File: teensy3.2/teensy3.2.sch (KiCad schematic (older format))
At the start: 30 parts

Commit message: ERC ok
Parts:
- removed Y?: 16 MHz, symbol Device:Crystal
- added C10, C11, C5, C6, C7: 0.1uF, symbol Device:CP_Small
- added C8, C9: 2.2uF, symbol Device:CP_Small
- added FB1, FB2: Ferrite, symbol Device:Ferrite_Bead
- added J12: AGND, TestPoint:TestPoint_Bridge_Pitch2.0mm_Drill0.7mm, symbol Connector_Generic:Conn_01x01
- added J13: AREF, TestPoint:TestPoint_Bridge_Pitch2.0mm_Drill0.7mm, symbol Connector_Generic:Conn_01x01
- added J14: 31, TestPoint:TestPoint_Bridge_Pitch2.0mm_Drill0.7mm, symbol Connector_Generic:Conn_01x01
- added J15: 26, TestPoint:TestPoint_Bridge_Pitch2.0mm_Drill0.7mm, symbol Connector_Generic:Conn_01x01
- added J16: A10, TestPoint:TestPoint_Bridge_Pitch2.0mm_Drill0.7mm, symbol Connector_Generic:Conn_01x01
- added J17: A11, TestPoint:TestPoint_Bridge_Pitch2.0mm_Drill0.7mm, symbol Connector_Generic:Conn_01x01
- added J18: A12, TestPoint:TestPoint_Bridge_Pitch2.0mm_Drill0.7mm, symbol Connector_Generic:Conn_01x01
- added J19: A13, TestPoint:TestPoint_Bridge_Pitch2.0mm_Drill0.7mm, symbol Connector_Generic:Conn_01x01
- added J20: 33, TestPoint:TestPoint_Bridge_Pitch2.0mm_Drill0.7mm, symbol Connector_Generic:Conn_01x01
- added J21: 24, TestPoint:TestPoint_Bridge_Pitch2.0mm_Drill0.7mm, symbol Connector_Generic:Conn_01x01
- added J22: 3, TestPoint:TestPoint_Bridge_Pitch2.0mm_Drill0.7mm, symbol Connector_Generic:Conn_01x01
- added J23: 4, TestPoint:TestPoint_Bridge_Pitch2.0mm_Drill0.7mm, symbol Connector_Generic:Conn_01x01
- added J25: DAC/A14, TestPoint:TestPoint_Bridge_Pitch2.0mm_Drill0.7mm, symbol Connector_Generic:Conn_01x01
- added J26: 16/A2, TestPoint:TestPoint_Bridge_Pitch2.0mm_Drill0.7mm, symbol Connector_Generic:Conn_01x01
- added J27: 17/A3, TestPoint:TestPoint_Bridge_Pitch2.0mm_Drill0.7mm, symbol Connector_Generic:Conn_01x01
- added J28: 19/A5, TestPoint:TestPoint_Bridge_Pitch2.0mm_Drill0.7mm, symbol Connector_Generic:Conn_01x01
- added J29: 18/A4, TestPoint:TestPoint_Bridge_Pitch2.0mm_Drill0.7mm, symbol Connector_Generic:Conn_01x01
- added J30: 0, TestPoint:TestPoint_Bridge_Pitch2.0mm_Drill0.7mm, symbol Connector_Generic:Conn_01x01
- added J31: 1, TestPoint:TestPoint_Bridge_Pitch2.0mm_Drill0.7mm, symbol Connector_Generic:Conn_01x01
- added J32: 32, TestPoint:TestPoint_Bridge_Pitch2.0mm_Drill0.7mm, symbol Connector_Generic:Conn_01x01
- added J33: 25, TestPoint:TestPoint_Bridge_Pitch2.0mm_Drill0.7mm, symbol Connector_Generic:Conn_01x01
- added J34: 15/A1, TestPoint:TestPoint_Bridge_Pitch2.0mm_Drill0.7mm, symbol Connector_Generic:Conn_01x01
- added J35: 22/A8, TestPoint:TestPoint_Bridge_Pitch2.0mm_Drill0.7mm, symbol Connector_Generic:Conn_01x01
- added J36: 23/A9, TestPoint:TestPoint_Bridge_Pitch2.0mm_Drill0.7mm, symbol Connector_Generic:Conn_01x01
- added J37: 9, TestPoint:TestPoint_Bridge_Pitch2.0mm_Drill0.7mm, symbol Connector_Generic:Conn_01x01
- added J38: 10, TestPoint:TestPoint_Bridge_Pitch2.0mm_Drill0.7mm, symbol Connector_Generic:Conn_01x01
- added J39: 11, TestPoint:TestPoint_Bridge_Pitch2.0mm_Drill0.7mm, symbol Connector_Generic:Conn_01x01
- added J40: 12, TestPoint:TestPoint_Bridge_Pitch2.0mm_Drill0.7mm, symbol Connector_Generic:Conn_01x01
- added J41: 28, TestPoint:TestPoint_Bridge_Pitch2.0mm_Drill0.7mm, symbol Connector_Generic:Conn_01x01
- added J42: 27, TestPoint:TestPoint_Bridge_Pitch2.0mm_Drill0.7mm, symbol Connector_Generic:Conn_01x01
- added J43: 29, TestPoint:TestPoint_Bridge_Pitch2.0mm_Drill0.7mm, symbol Connector_Generic:Conn_01x01
- added J44: 30, TestPoint:TestPoint_Bridge_Pitch2.0mm_Drill0.7mm, symbol Connector_Generic:Conn_01x01
- added J45: 2, TestPoint:TestPoint_Bridge_Pitch2.0mm_Drill0.7mm, symbol Connector_Generic:Conn_01x01
- added J46: 14/A0, TestPoint:TestPoint_Bridge_Pitch2.0mm_Drill0.7mm, symbol Connector_Generic:Conn_01x01
- added J47: 7, TestPoint:TestPoint_Bridge_Pitch2.0mm_Drill0.7mm, symbol Connector_Generic:Conn_01x01
- added J48: 8, TestPoint:TestPoint_Bridge_Pitch2.0mm_Drill0.7mm, symbol Connector_Generic:Conn_01x01
- added J49: 6, TestPoint:TestPoint_Bridge_Pitch2.0mm_Drill0.7mm, symbol Connector_Generic:Conn_01x01
- added J50: 20/A6, TestPoint:TestPoint_Bridge_Pitch2.0mm_Drill0.7mm, symbol Connector_Generic:Conn_01x01
- added J51: 21/A7, TestPoint:TestPoint_Bridge_Pitch2.0mm_Drill0.7mm, symbol Connector_Generic:Conn_01x01
- added J52: 5, TestPoint:TestPoint_Bridge_Pitch2.0mm_Drill0.7mm, symbol Connector_Generic:Conn_01x01
- added J7: 3.3V, TestPoint:TestPoint_Bridge_Pitch2.0mm_Drill0.7mm, symbol Connector_Generic:Conn_01x01
- added R3: 470, symbol Device:R
- added Y2: 16 MHz, symbol Device:Crystal
- gave numbers to parts that had none: 29
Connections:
- net labels added: GNDA, PTA0, PTA1, PTA2, PTA3, VBAT
- wire segments 110 -> 197
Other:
- moved on the sheet: C1, C2, C3, C4, D1, D2, D3, F1, J1, J10, J11, J2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

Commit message: asignacion de footprints lista
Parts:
- removed D1, D2: 1A, symbol Device:D
- removed FB1, FB2: Ferrite, symbol Device:Ferrite_Bead
- removed J10, J9: GND, TestPoint:TestPoint_Bridge_Pitch2.0mm_Drill0.7mm, symbol Connector_Generic:Conn_01x01
- removed J11: PROG, TestPoint:TestPoint_Bridge_Pitch2.0mm_Drill0.7mm, symbol Connector_Generic:Conn_01x01
- removed J12: AGND, TestPoint:TestPoint_Bridge_Pitch2.0mm_Drill0.7mm, symbol Connector_Generic:Conn_01x01
- removed J13: AREF, TestPoint:TestPoint_Bridge_Pitch2.0mm_Drill0.7mm, symbol Connector_Generic:Conn_01x01
- removed J14: 31, TestPoint:TestPoint_Bridge_Pitch2.0mm_Drill0.7mm, symbol Connector_Generic:Conn_01x01
- removed J15: 26, TestPoint:TestPoint_Bridge_Pitch2.0mm_Drill0.7mm, symbol Connector_Generic:Conn_01x01
- removed J16: A10, TestPoint:TestPoint_Bridge_Pitch2.0mm_Drill0.7mm, symbol Connector_Generic:Conn_01x01
- removed J17: A11, TestPoint:TestPoint_Bridge_Pitch2.0mm_Drill0.7mm, symbol Connector_Generic:Conn_01x01
- removed J18: A12, TestPoint:TestPoint_Bridge_Pitch2.0mm_Drill0.7mm, symbol Connector_Generic:Conn_01x01
- removed J19: A13, TestPoint:TestPoint_Bridge_Pitch2.0mm_Drill0.7mm, symbol Connector_Generic:Conn_01x01
- removed J20: 33, TestPoint:TestPoint_Bridge_Pitch2.0mm_Drill0.7mm, symbol Connector_Generic:Conn_01x01
- removed J21: 24, TestPoint:TestPoint_Bridge_Pitch2.0mm_Drill0.7mm, symbol Connector_Generic:Conn_01x01
- removed J22: 3, TestPoint:TestPoint_Bridge_Pitch2.0mm_Drill0.7mm, symbol Connector_Generic:Conn_01x01
- removed J23: 4, TestPoint:TestPoint_Bridge_Pitch2.0mm_Drill0.7mm, symbol Connector_Generic:Conn_01x01
- removed J24: RESET, TestPoint:TestPoint_Bridge_Pitch2.0mm_Drill0.7mm, symbol Connector_Generic:Conn_01x01
- removed J25: DAC/A14, TestPoint:TestPoint_Bridge_Pitch2.0mm_Drill0.7mm, symbol Connector_Generic:Conn_01x01
- removed J26: 16/A2, TestPoint:TestPoint_Bridge_Pitch2.0mm_Drill0.7mm, symbol Connector_Generic:Conn_01x01
- removed J27: 17/A3, TestPoint:TestPoint_Bridge_Pitch2.0mm_Drill0.7mm, symbol Connector_Generic:Conn_01x01
- removed J28: 19/A5, TestPoint:TestPoint_Bridge_Pitch2.0mm_Drill0.7mm, symbol Connector_Generic:Conn_01x01
- removed J29: 18/A4, TestPoint:TestPoint_Bridge_Pitch2.0mm_Drill0.7mm, symbol Connector_Generic:Conn_01x01
- removed J3: VUSB, TestPoint:TestPoint_Bridge_Pitch2.0mm_Drill0.7mm, symbol Connector_Generic:Conn_01x01
- removed J30: 0, TestPoint:TestPoint_Bridge_Pitch2.0mm_Drill0.7mm, symbol Connector_Generic:Conn_01x01
- removed J31: 1, TestPoint:TestPoint_Bridge_Pitch2.0mm_Drill0.7mm, symbol Connector_Generic:Conn_01x01
- removed J32: 32, TestPoint:TestPoint_Bridge_Pitch2.0mm_Drill0.7mm, symbol Connector_Generic:Conn_01x01
- removed J33: 25, TestPoint:TestPoint_Bridge_Pitch2.0mm_Drill0.7mm, symbol Connector_Generic:Conn_01x01
- removed J34: 15/A1, TestPoint:TestPoint_Bridge_Pitch2.0mm_Drill0.7mm, symbol Connector_Generic:Conn_01x01
- removed J35: 22/A8, TestPoint:TestPoint_Bridge_Pitch2.0mm_Drill0.7mm, symbol Connector_Generic:Conn_01x01
- removed J36: 23/A9, TestPoint:TestPoint_Bridge_Pitch2.0mm_Drill0.7mm, symbol Connector_Generic:Conn_01x01
- removed J37: 9, TestPoint:TestPoint_Bridge_Pitch2.0mm_Drill0.7mm, symbol Connector_Generic:Conn_01x01
- removed J38: 10, TestPoint:TestPoint_Bridge_Pitch2.0mm_Drill0.7mm, symbol Connector_Generic:Conn_01x01
- removed J39: 11, TestPoint:TestPoint_Bridge_Pitch2.0mm_Drill0.7mm, symbol Connector_Generic:Conn_01x01
- removed J40: 12, TestPoint:TestPoint_Bridge_Pitch2.0mm_Drill0.7mm, symbol Connector_Generic:Conn_01x01
- removed J41: 28, TestPoint:TestPoint_Bridge_Pitch2.0mm_Drill0.7mm, symbol Connector_Generic:Conn_01x01
- removed J42: 27, TestPoint:TestPoint_Bridge_Pitch2.0mm_Drill0.7mm, symbol Connector_Generic:Conn_01x01
- removed J43: 29, TestPoint:TestPoint_Bridge_Pitch2.0mm_Drill0.7mm, symbol Connector_Generic:Conn_01x01
- removed J44: 30, TestPoint:TestPoint_Bridge_Pitch2.0mm_Drill0.7mm, symbol Connector_Generic:Conn_01x01
- removed J45: 2, TestPoint:TestPoint_Bridge_Pitch2.0mm_Drill0.7mm, symbol Connector_Generic:Conn_01x01
- removed J46: 14/A0, TestPoint:TestPoint_Bridge_Pitch2.0mm_Drill0.7mm, symbol Connector_Generic:Conn_01x01
- removed J47: 7, TestPoint:TestPoint_Bridge_Pitch2.0mm_Drill0.7mm, symbol Connector_Generic:Conn_01x01
- removed J48: 8, TestPoint:TestPoint_Bridge_Pitch2.0mm_Drill0.7mm, symbol Connector_Generic:Conn_01x01
- removed J49: 6, TestPoint:TestPoint_Bridge_Pitch2.0mm_Drill0.7mm, symbol Connector_Generic:Conn_01x01
- removed J5, J7: 3.3V, TestPoint:TestPoint_Bridge_Pitch2.0mm_Drill0.7mm, symbol Connector_Generic:Conn_01x01
- removed J50: 20/A6, TestPoint:TestPoint_Bridge_Pitch2.0mm_Drill0.7mm, symbol Connector_Generic:Conn_01x01
- removed J51: 21/A7, TestPoint:TestPoint_Bridge_Pitch2.0mm_Drill0.7mm, symbol Connector_Generic:Conn_01x01
- removed J52: 5, TestPoint:TestPoint_Bridge_Pitch2.0mm_Drill0.7mm, symbol Connector_Generic:Conn_01x01
- removed J53: 13 (LED), TestPoint:TestPoint_Bridge_Pitch2.0mm_Drill0.7mm, symbol Connector_Generic:Conn_01x01
- removed J6: VIN, TestPoint:TestPoint_Bridge_Pitch2.0mm_Drill0.7mm, symbol Connector_Generic:Conn_01x01
- removed JP1: Split VIN-VUSB, symbol Device:Jumper_NC_Small
- added D1: PMEG4010CPA, Package_SON:HUSON-3-1EP_2x2mm_P1.3mm_EP1.1x1.6mm, symbol Device:D_Schottky_x2_KCom_AAK
- added JP1: Split VIN-VUSB, Jumper:SolderJumper-2_P1.3mm_Bridged2Bar_Pad1.0x1.5mm, symbol Jumper:SolderJumper_2_Bridged
- added L1, L2: Ferrite, Inductor_SMD:L_0201_0603Metric, symbol Device:L_Core_Ferrite
- added TP10: PROG, TestPoint:TestPoint_THTPad_D2.0mm_Drill1.0mm, symbol Connector:TestPoint
- added TP11: AGND, TestPoint:TestPoint_THTPad_D2.0mm_Drill1.0mm, symbol Connector:TestPoint
- added TP12: AREF, TestPoint:TestPoint_THTPad_D2.0mm_Drill1.0mm, symbol Connector:TestPoint
- added TP13: RESET, TestPoint:TestPoint_THTPad_D2.0mm_Drill1.0mm, symbol Connector:TestPoint
- added TP14: 31, TestPoint:TestPoint_THTPad_D2.0mm_Drill1.0mm, symbol Connector:TestPoint
- added TP15: 26, TestPoint:TestPoint_THTPad_D2.0mm_Drill1.0mm, symbol Connector:TestPoint
- added TP16: A10, TestPoint:TestPoint_THTPad_D2.0mm_Drill1.0mm, symbol Connector:TestPoint
- added TP17: A11, TestPoint:TestPoint_THTPad_D2.0mm_Drill1.0mm, symbol Connector:TestPoint
- added TP18: A12, TestPoint:TestPoint_THTPad_D2.0mm_Drill1.0mm, symbol Connector:TestPoint
- added TP19: A13, TestPoint:TestPoint_THTPad_D2.0mm_Drill1.0mm, symbol Connector:TestPoint
- added TP2: VUSB, TestPoint:TestPoint_THTPad_D2.0mm_Drill1.0mm, symbol Connector:TestPoint
- added TP20: 33, TestPoint:TestPoint_THTPad_D2.0mm_Drill1.0mm, symbol Connector:TestPoint
- added TP21: 24, TestPoint:TestPoint_THTPad_D2.0mm_Drill1.0mm, symbol Connector:TestPoint
- added TP22: 3, TestPoint:TestPoint_THTPad_D2.0mm_Drill1.0mm, symbol Connector:TestPoint
- added TP23: 4, TestPoint:TestPoint_THTPad_D2.0mm_Drill1.0mm, symbol Connector:TestPoint
- added TP24: DAC/A14, TestPoint:TestPoint_THTPad_D2.0mm_Drill1.0mm, symbol Connector:TestPoint
- added TP25: 16/A2, TestPoint:TestPoint_THTPad_D2.0mm_Drill1.0mm, symbol Connector:TestPoint
- added TP26: 17/A3, TestPoint:TestPoint_THTPad_D2.0mm_Drill1.0mm, symbol Connector:TestPoint
- added TP27: 19/A5, TestPoint:TestPoint_THTPad_D2.0mm_Drill1.0mm, symbol Connector:TestPoint
- added TP28: 18/A4, TestPoint:TestPoint_THTPad_D2.0mm_Drill1.0mm, symbol Connector:TestPoint
- added TP29: 0, TestPoint:TestPoint_THTPad_D2.0mm_Drill1.0mm, symbol Connector:TestPoint
- added TP30: 1, TestPoint:TestPoint_THTPad_D2.0mm_Drill1.0mm, symbol Connector:TestPoint
- added TP31: 32, TestPoint:TestPoint_THTPad_D2.0mm_Drill1.0mm, symbol Connector:TestPoint
- added TP32: 25, TestPoint:TestPoint_THTPad_D2.0mm_Drill1.0mm, symbol Connector:TestPoint
- added TP33: 15/A1, TestPoint:TestPoint_THTPad_D2.0mm_Drill1.0mm, symbol Connector:TestPoint
- added TP34: 22/A8, TestPoint:TestPoint_THTPad_D2.0mm_Drill1.0mm, symbol Connector:TestPoint
- added TP35: 23/A9, TestPoint:TestPoint_THTPad_D2.0mm_Drill1.0mm, symbol Connector:TestPoint
- added TP36: 9, TestPoint:TestPoint_THTPad_D2.0mm_Drill1.0mm, symbol Connector:TestPoint
- added TP37: 10, TestPoint:TestPoint_THTPad_D2.0mm_Drill1.0mm, symbol Connector:TestPoint
- added TP38: 11, TestPoint:TestPoint_THTPad_D2.0mm_Drill1.0mm, symbol Connector:TestPoint
- added TP39: 12, TestPoint:TestPoint_THTPad_D2.0mm_Drill1.0mm, symbol Connector:TestPoint
- added TP4, TP6: 3.3V, TestPoint:TestPoint_THTPad_D2.0mm_Drill1.0mm, symbol Connector:TestPoint
- added TP40: 28, TestPoint:TestPoint_THTPad_D2.0mm_Drill1.0mm, symbol Connector:TestPoint
- added TP41: 27, TestPoint:TestPoint_THTPad_D2.0mm_Drill1.0mm, symbol Connector:TestPoint
- added TP42: 29, TestPoint:TestPoint_THTPad_D2.0mm_Drill1.0mm, symbol Connector:TestPoint
- added TP43: 30, TestPoint:TestPoint_THTPad_D2.0mm_Drill1.0mm, symbol Connector:TestPoint
- added TP44: 2, TestPoint:TestPoint_THTPad_D2.0mm_Drill1.0mm, symbol Connector:TestPoint
- added TP45: 14/A0, TestPoint:TestPoint_THTPad_D2.0mm_Drill1.0mm, symbol Connector:TestPoint
- added TP46: 7, TestPoint:TestPoint_THTPad_D2.0mm_Drill1.0mm, symbol Connector:TestPoint
- added TP47: 8, TestPoint:TestPoint_THTPad_D2.0mm_Drill1.0mm, symbol Connector:TestPoint
- added TP48: 6, TestPoint:TestPoint_THTPad_D2.0mm_Drill1.0mm, symbol Connector:TestPoint
- added TP49: 20/A6, TestPoint:TestPoint_THTPad_D2.0mm_Drill1.0mm, symbol Connector:TestPoint
- added TP5: VIN, TestPoint:TestPoint_THTPad_D2.0mm_Drill1.0mm, symbol Connector:TestPoint
- added TP50: 21/A7, TestPoint:TestPoint_THTPad_D2.0mm_Drill1.0mm, symbol Connector:TestPoint
- added TP51: 5, TestPoint:TestPoint_THTPad_D2.0mm_Drill1.0mm, symbol Connector:TestPoint
- added TP52: 13 (LED), TestPoint:TestPoint_THTPad_D2.0mm_Drill1.0mm, symbol Connector:TestPoint
- added TP8, TP9: GND, TestPoint:TestPoint_THTPad_D2.0mm_Drill1.0mm, symbol Connector:TestPoint
- C1, C10, C11, C5, C6, C7: footprint (none) -> Capacitor_SMD:C_0603_1608Metric
- C2, C3, C4, C8, C9: footprint (none) -> Capacitor_SMD:C_0805_2012Metric
- D2: renamed from D3; footprint (none) -> LED_SMD:LED_0805_2012Metric
- F1: footprint (none) -> Fuse:Fuse_0805_2012Metric
- J2: footprint (none) -> Connector_USB:USB_Micro-B_Molex_47346-0001
- R1, R2, R3, R4: footprint (none) -> Resistor_SMD:R_0201_0603Metric
- SW1: footprint (none) -> Button_Switch_SMD:SW_SPST_PTS810
- TP1: renamed from J1; footprint TestPoint:TestPoint_Bridge_Pitch2.0mm_Drill0.7mm -> TestPoint:TestPoint_THTPad_D2.0mm_Drill1.0mm; symbol Connector_Generic:Conn_01x01 -> Connector:TestPoint
- TP3: renamed from J4; footprint TestPoint:TestPoint_Bridge_Pitch2.0mm_Drill0.7mm -> TestPoint:TestPoint_THTPad_D2.0mm_Drill1.0mm; symbol Connector_Generic:Conn_01x01 -> Connector:TestPoint
- TP7: renamed from J8; footprint TestPoint:TestPoint_Bridge_Pitch2.0mm_Drill0.7mm -> TestPoint:TestPoint_THTPad_D2.0mm_Drill1.0mm; symbol Connector_Generic:Conn_01x01 -> Connector:TestPoint
- U3: footprint (none) -> Package_QFP:LQFP-64_10x10mm_P0.5mm
- Y1: footprint (none) -> Crystal:Crystal_SMD_TXC_AX_8045-2Pin_8.0x4.5mm
- Y2: footprint (none) -> Crystal:Crystal_SMD_HC49-SD
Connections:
- wire segments 197 -> 196
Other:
- moved on the sheet: C1, C2, C5, C6, C7, C8

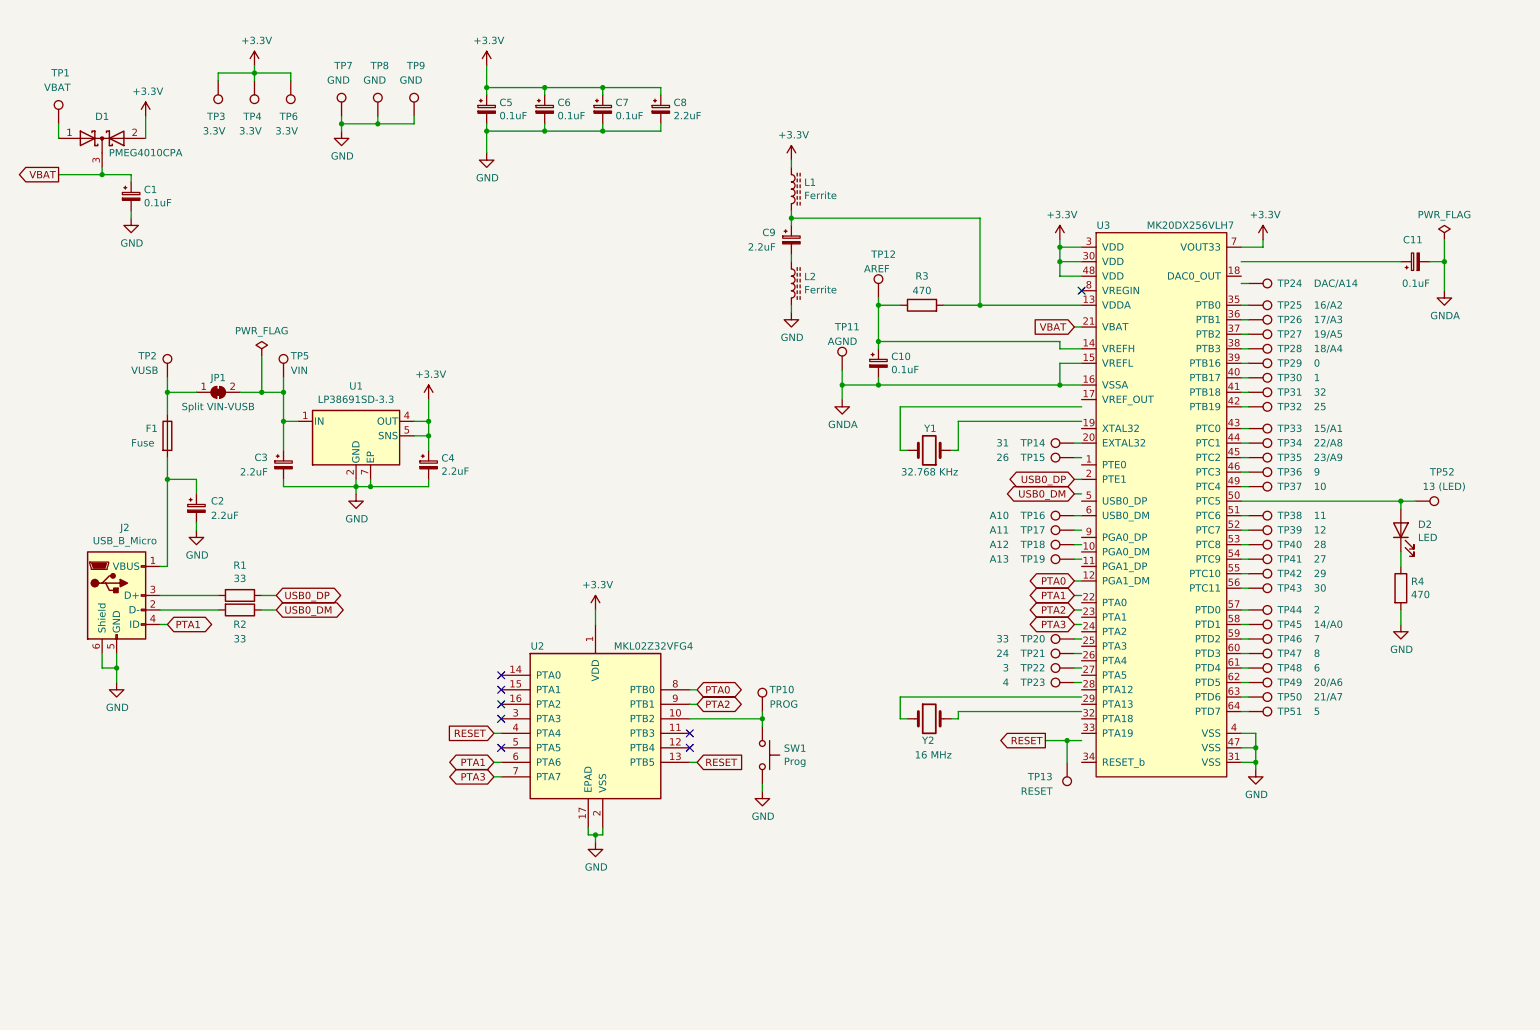
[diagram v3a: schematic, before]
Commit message: ajustes al esquematico
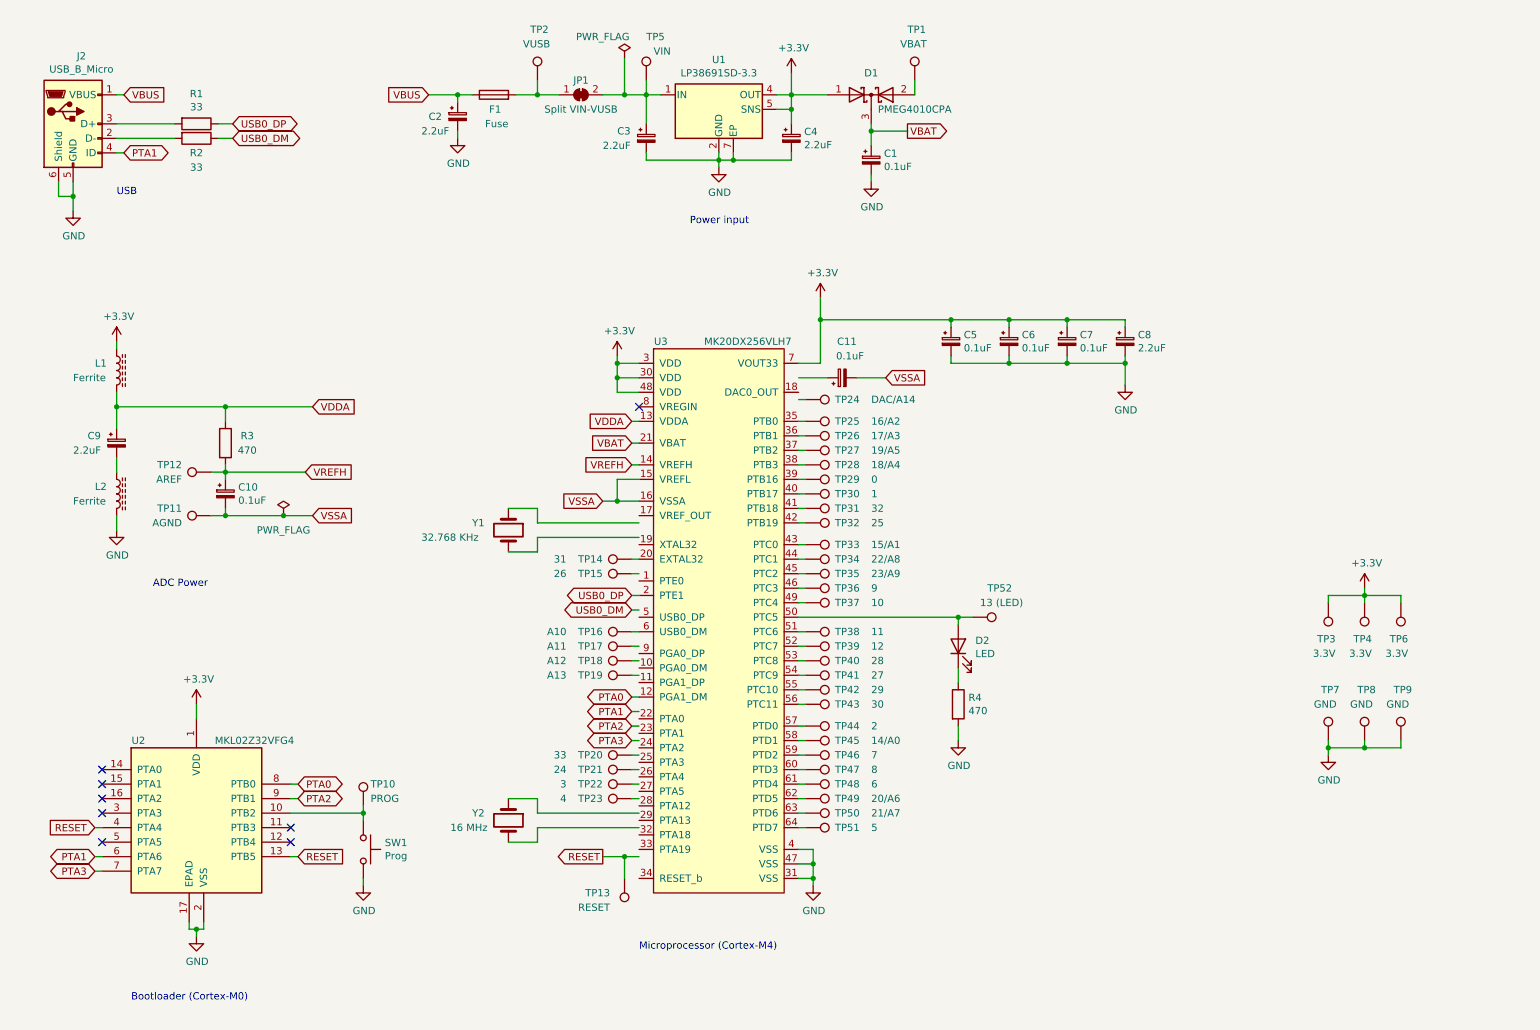
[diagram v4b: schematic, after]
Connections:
- net labels added: VBUS, VDDA, VREFH, VSSA
- net labels removed: GNDA
- wire segments 196 -> 190
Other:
- note added: "ADC Power"
- note added: "Bootloader (Cortex-M0)"
- note added: "Microprocessor (Cortex-M4)"
- note added: "Power input"
- note added: "USB"
- moved on the sheet: C1, C10, C11, C2, C3, C4, C5, C6, C7, C8, C9, D1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
